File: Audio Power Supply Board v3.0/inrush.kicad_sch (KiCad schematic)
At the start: 4 parts, among them Q1 IPDD60R080G7

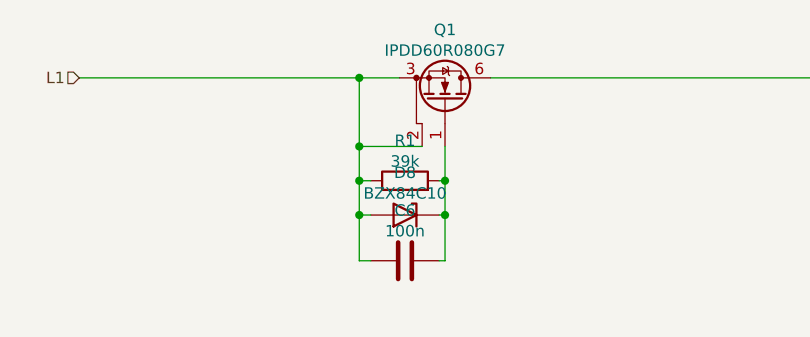
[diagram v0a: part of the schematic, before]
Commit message: Change to a modular drawing and design
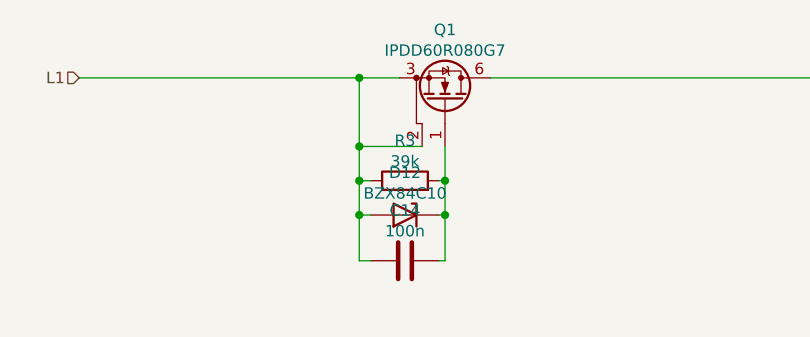
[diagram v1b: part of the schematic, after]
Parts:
- renumbered C6 to C14, D8 to D12, R1 to R3
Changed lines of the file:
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@@
   (symbol (lib_id "Device:R") (at 177.8 62.23 90) (unit 1)
     (in_bom yes) (on_board yes)
-    (property "Reference" "R1" (id 0) (at 177.8 57.7808 90))
+    (property "Reference" "R3" (id 0) (at 177.8 57.7808 90))
     (property "Value" "39k" (id 1) (at 177.8 60.0795 90))
     (property "Footprint" "" (id 2) (at 177.8 64.008 90)
@@
   (symbol (lib_id "Diode:BZX84Cxx") (at 177.8 66.04 0) (mirror y) (unit 1)
     (in_bom yes) (on_board yes)
-    (property "Reference" "D8" (id 0) (at 177.8 61.3368 0))
+    (property "Reference" "D12" (id 0) (at 177.8 61.3368 0))
     (property "Value" "BZX84C10" (id 1) (at 177.8 63.6355 0))
     (property "Footprint" "Diode_SMD:D_SOT-23_ANK" (id 2) (at 177.8 70.485 0)
@@
   (symbol (lib_id "Device:C") (at 177.8 71.12 90) (unit 1)
     (in_bom yes) (on_board yes)
-    (property "Reference" "C6" (id 0) (at 177.8 65.5278 90))
+    (property "Reference" "C14" (id 0) (at 177.8 65.5278 90))
     (property "Value" "100n" (id 1) (at 177.8 67.8265 90))
     (property "Footprint" "" (id 2) (at 181.61 70.1548 0)

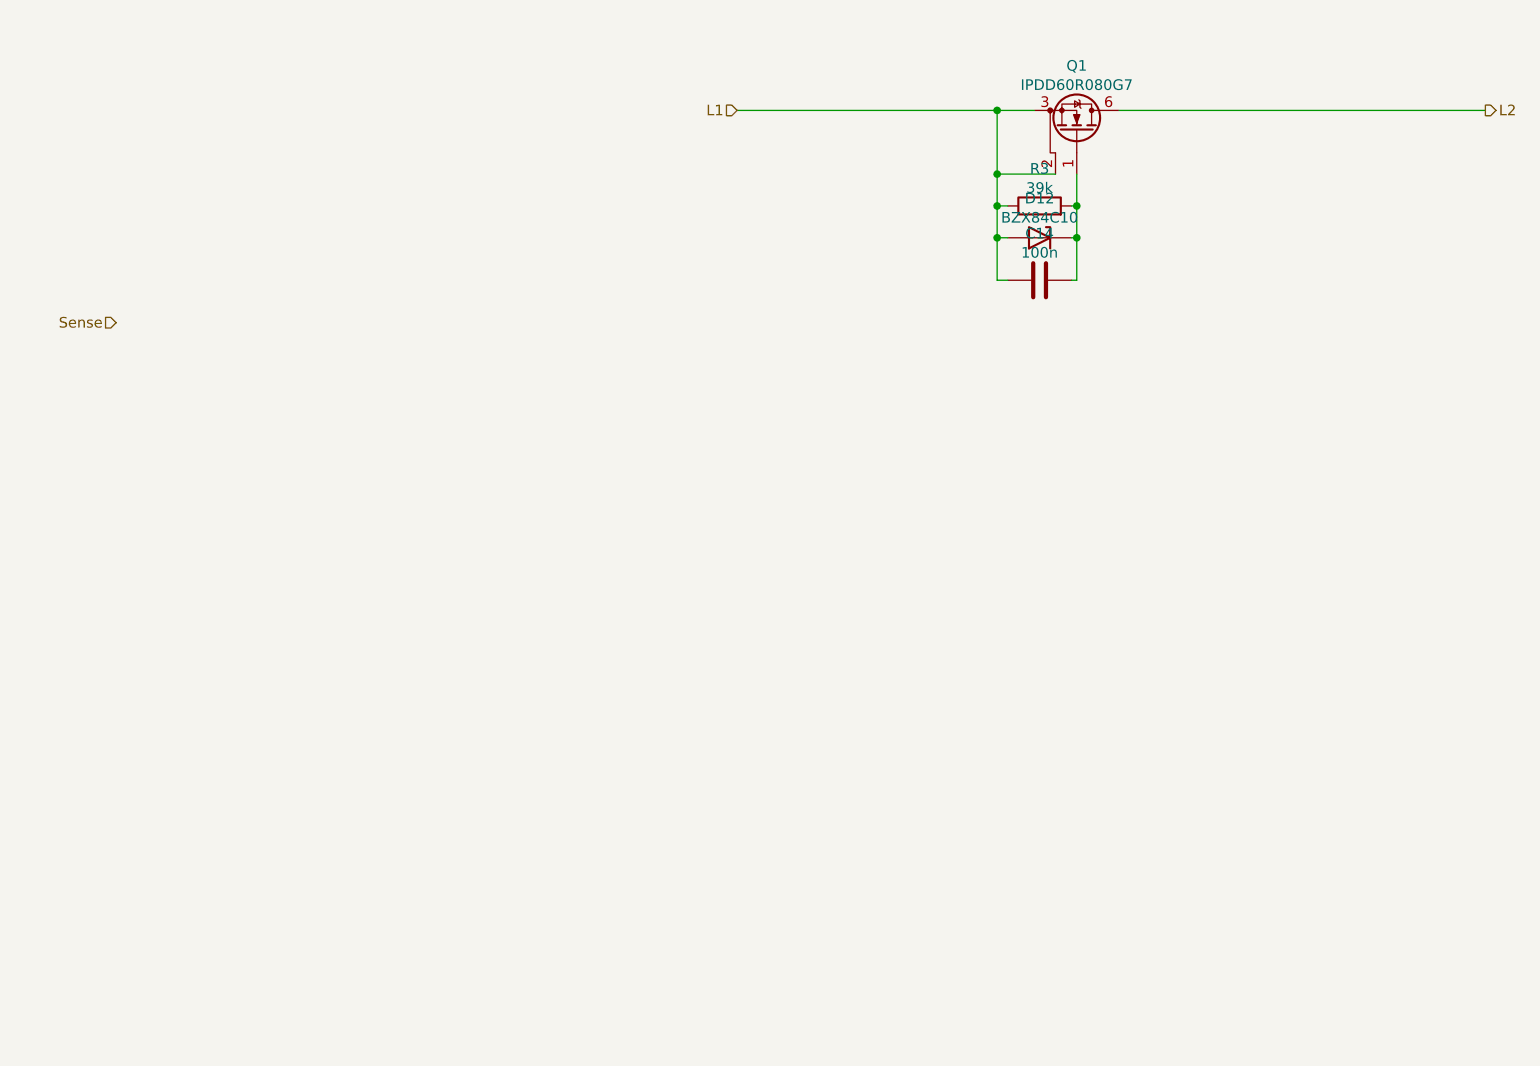
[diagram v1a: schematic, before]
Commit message: Add protection circuits
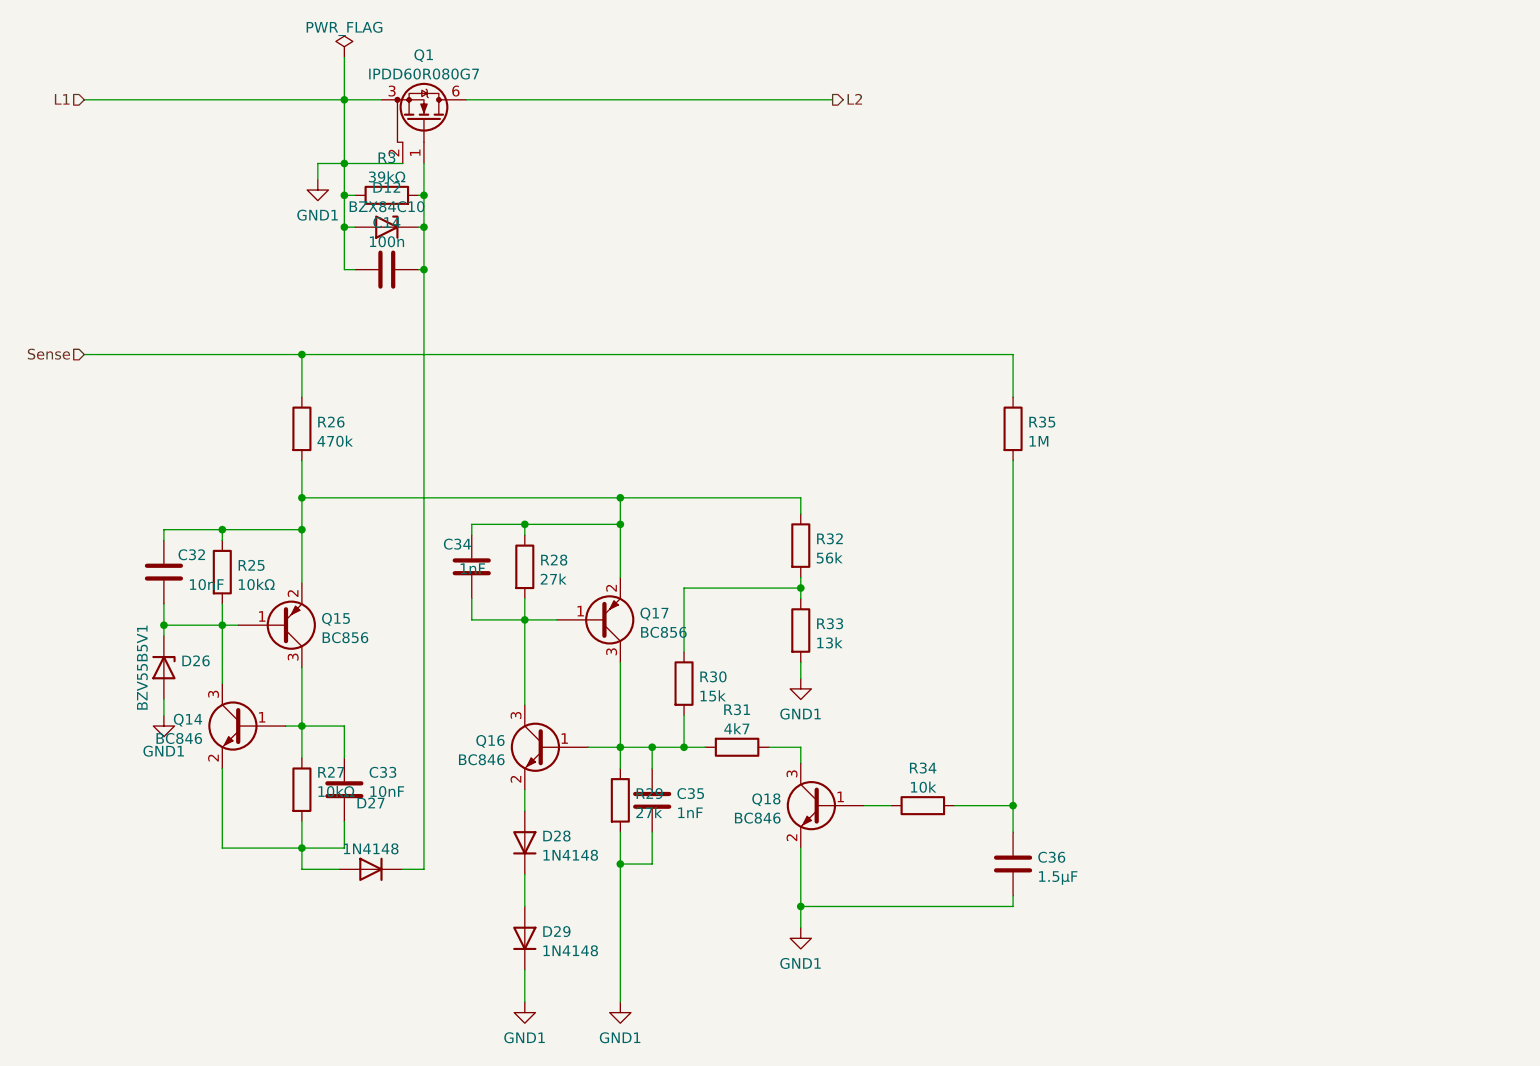
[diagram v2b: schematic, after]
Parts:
- added C32, C33: 10nF, symbol Device:C
- added C34, C35: 1nF, symbol Device:C
- added C36: 1.5µF, symbol Device:C
- added D26: BZV55B5V1, Diode_SMD:D_MiniMELF, symbol Diode:BZV55B5V1
- added D27, D28, D29: 1N4148, Diode_THT:D_DO-35_SOD27_P7.62mm_Horizontal, symbol Diode:1N4148
- added Q14, Q16, Q18: BC846, Package_TO_SOT_SMD:SOT-23, symbol Transistor_BJT:BC846
- added Q15, Q17: BC856, Package_TO_SOT_SMD:SOT-23, symbol Transistor_BJT:BC856
- added R25, R27: 10kΩ, Resistor_THT:R_Axial_DIN0207_L6.3mm_D2.5mm_P7.62mm_Horizontal, symbol Device:R
- added R26: 470k, Resistor_THT:R_Axial_DIN0207_L6.3mm_D2.5mm_P7.62mm_Horizontal, symbol Device:R
- added R28, R29: 27k, Resistor_THT:R_Axial_DIN0207_L6.3mm_D2.5mm_P7.62mm_Horizontal, symbol Device:R
- added R30: 15k, Resistor_THT:R_Axial_DIN0207_L6.3mm_D2.5mm_P7.62mm_Horizontal, symbol Device:R
- added R31: 4k7, Resistor_THT:R_Axial_DIN0207_L6.3mm_D2.5mm_P7.62mm_Horizontal, symbol Device:R
- added R32: 56k, Resistor_THT:R_Axial_DIN0207_L6.3mm_D2.5mm_P7.62mm_Horizontal, symbol Device:R
- added R33: 13k, Resistor_THT:R_Axial_DIN0207_L6.3mm_D2.5mm_P7.62mm_Horizontal, symbol Device:R
- added R34: 10k, Resistor_THT:R_Axial_DIN0207_L6.3mm_D2.5mm_P7.62mm_Horizontal, symbol Device:R
- added R35: 1M, Resistor_THT:R_Axial_DIN0207_L6.3mm_D2.5mm_P7.62mm_Horizontal, symbol Device:R
- R3: value 39k -> 39kΩ
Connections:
- net Sense: now also R26.1, R35.1
- net at C14.2, D12.1 (K), Q1.1 (G)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: now also D27.1 (K)
- net L1 renamed GND1
- net GND1: now also C35.2, C36.2, D26.2 (A), D29.1 (K), Q18.2 (E), R29.2, R33.2
- new net: C35.1, Q16.1 (B), Q17.3 (C), R29.1, R30.2, R31.2
- new net: C32.1, C34.1, Q15.2 (E), Q17.2 (E), R25.1, R26.2, R28.1, R32.1
- new net: C36.1, R34.2, R35.2
- new net: D28.1 (K), D29.2 (A)
- new net: D28.2 (A), Q16.2 (E)
- new net: Q18.3 (C), R31.1
- new net: R30.1, R32.2, R33.1
- new net: C34.2, Q16.3 (C), Q17.1 (B), R28.2
- new net: C32.2, D26.1 (K), Q14.3 (C), Q15.1 (B), R25.2
- new net: C33.1, Q14.1 (B), Q15.3 (C), R27.1
- new net: C33.2, D27.2 (A), Q14.2 (E), R27.2
- new net: Q18.1 (B), R34.1
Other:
- moved on the sheet: C14, D12, Q1, R3
